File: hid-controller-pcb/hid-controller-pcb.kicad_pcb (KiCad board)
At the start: 4 copper layers, 130.7 x 87.2 mm, 65 parts, among them IC1 RT9080-33GJ5, J1 10118194-0011LF, J2 Jumper, J3 STLink, U1 STM32F103C8Tx, U3 COM-09032, U4 COM-09032, Y1 8MHz, Y2 32.768KHz

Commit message: further work on controller
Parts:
- moved R13 145.3 mm to (255.9, 51.3), turned to 180 degrees
- moved C7 108.8 mm to (200.5, 55.7), turned to 90 degrees
- moved C12 99.0 mm to (212.4, 48.6), turned to -90 degrees
- moved R12 74.5 mm to (157.7, 49.4), turned to -90 degrees
- moved J2 68.7 mm to (205.1, 87.2), turned to 90 degrees
- moved S4 19.8 mm to (151.3, 49.4), turned to -90 degrees
- moved S2 19.5 mm to (170.9, 49.5)
- moved S10 9.44 mm to (208.0, 93.9)
- moved C2 7.12 mm to (214.2, 77.7)
- moved C3 7.12 mm to (214.2, 72.7)
- moved Y2 7.12 mm to (203.1, 74.6)
- moved C4 7.12 mm to (201.5, 69.3)
- moved C5 7.12 mm to (204.5, 69.3)
- moved Y1 7.12 mm to (210.5, 75.3)
- moved C9 5.83 mm to (191.5, 43.5)
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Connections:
- U1 pad 26: DPAD_1 -> BTN_RT
- U1 pad 31: BTN_RT -> DPAD_1
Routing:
- net AN_A1: track 0.00 -> 93.9 mm
- net AN_B1: track 0.00 -> 83.8 mm
- net DPAD_4: track 0.00 -> 79.3 mm, vias 0 -> 1
- net BTN_LT: track 0.00 -> 56.3 mm
- net DPAD_3: track 0.00 -> 55.9 mm, vias 0 -> 1
- net DPAD_1: track 0.00 -> 54.9 mm, vias 0 -> 1
- net AN_B2: track 0.00 -> 52.9 mm
- net DPAD_2: track 0.00 -> 42.7 mm, vias 0 -> 1
- net BOOT0: track 0.00 -> 42.3 mm, vias 0 -> 1
- net AN_A2: track 0.00 -> 36.2 mm
- net AN_SEL1: track 0.00 -> 33.1 mm
- net AN_SEL2: track 0.00 -> 32.1 mm
- net +3V3: track 76.9 -> 55.0 mm, vias 4 -> 7
- net BTN_LB: track 0.00 -> 7.78 mm, vias 0 -> 1
- net Net-(C5-Pad2): track 4.62 -> 12.4 mm
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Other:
- board text added: "SHARE"
- board text added: "START"

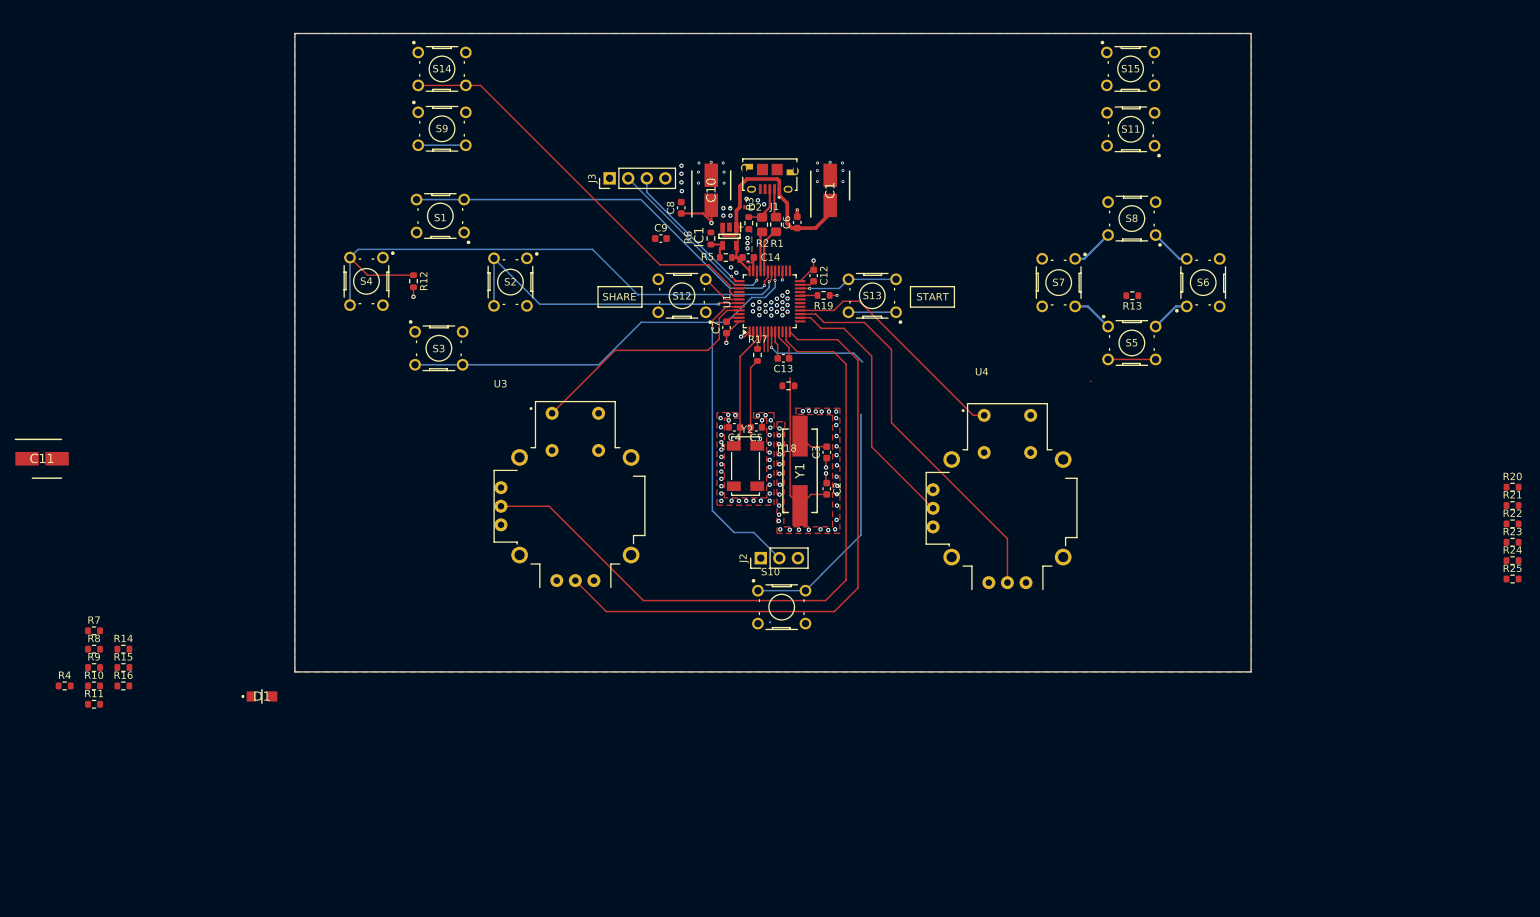
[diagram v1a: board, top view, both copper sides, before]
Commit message: Controller layout done! Reviewing before sending to JLC
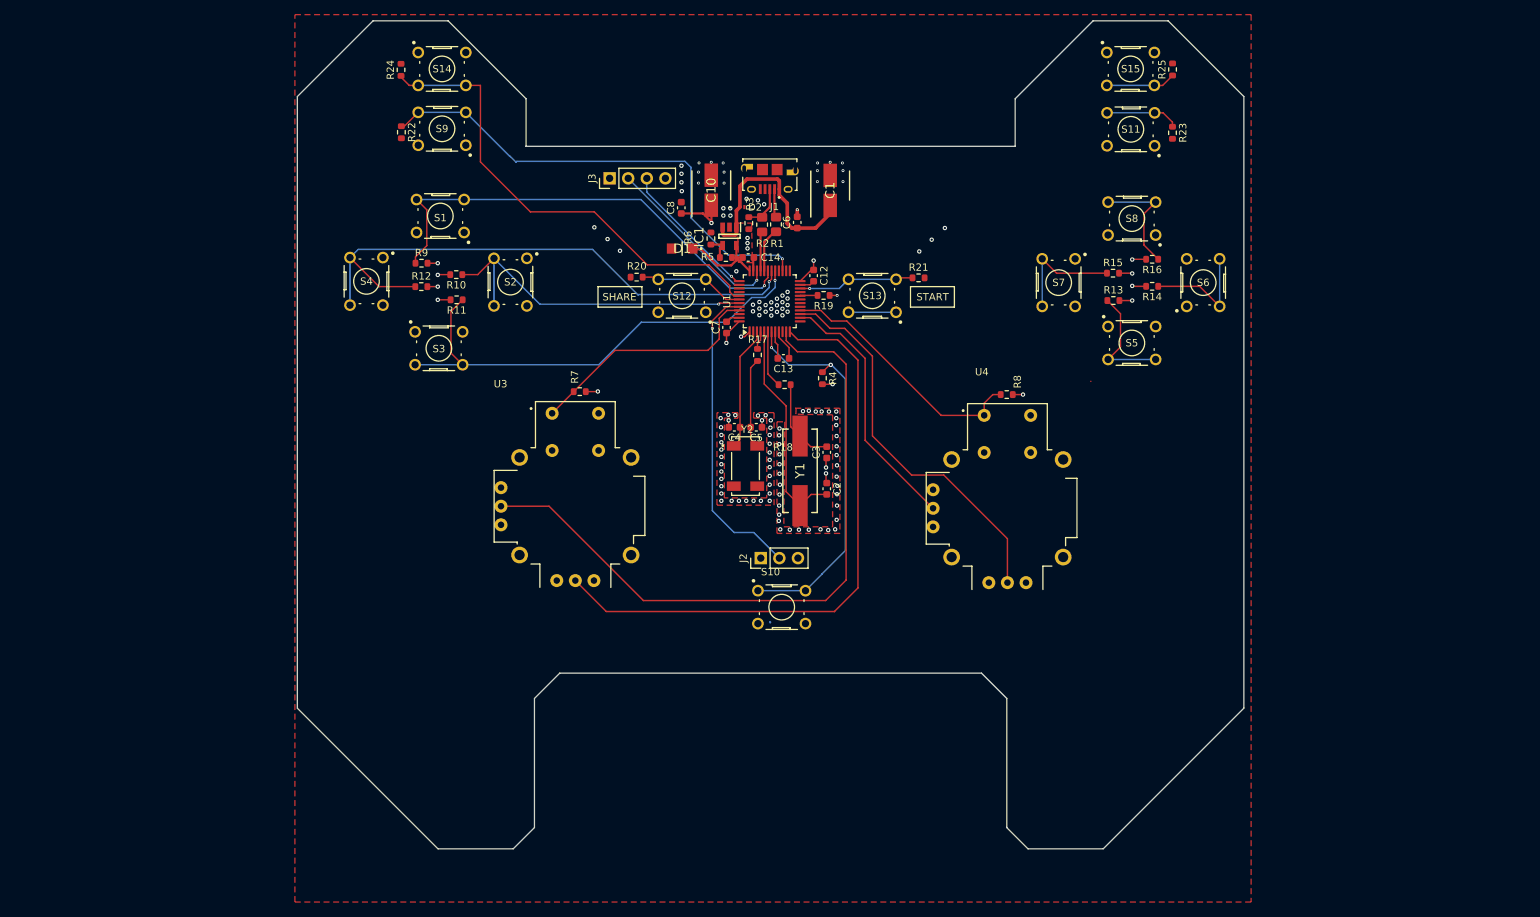
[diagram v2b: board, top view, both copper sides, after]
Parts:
- removed C11: 10uF, lib:CAPAE530X550N
- removed C9: 1uF, Capacitor_SMD:C_0603_1608Metric
- moved R24 166.0 mm to (156.0, 20.5), turned to 90 degrees
- moved R22 161.0 mm to (156.0, 29.0), turned to -90 degrees
- moved R16 152.2 mm to (258.6, 46.4), turned to 180 degrees
- moved R14 149.1 mm to (258.6, 50.1), turned to 180 degrees
- moved R15 145.6 mm to (253.3, 48.3)
- moved R8 129.5 mm to (238.8, 64.8), turned to 180 degrees
- moved R20 123.1 mm to (188.2, 48.8), turned to 180 degrees
- moved R4 111.8 mm to (213.6, 62.6), turned to -90 degrees
- moved R21 86.9 mm to (226.7, 48.9)
- moved D1 83.9 mm to (194.4, 44.9), turned to 180 degrees
- moved R25 83.7 mm to (261.4, 20.4), turned to 90 degrees
- moved R10 74.9 mm to (163.5, 48.5), turned to 180 degrees
- moved R11 74.2 mm to (163.6, 51.9), turned to 180 degrees
- moved R7 74.0 mm to (180.4, 64.5), turned to 180 degrees
- moved R23 72.7 mm to (261.4, 29.1), turned to -90 degrees
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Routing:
- net BTN_LB: track 7.78 -> 66.9 mm
- net BTN_3: track 0.00 -> 16.2 mm
- net BTN_2: track 0.00 -> 16.0 mm
- net BTN_4: track 0.00 -> 15.8 mm
- net GND: track 17.5 -> 29.9 mm, vias 122 -> 134
- net +3V3: track 55.0 -> 44.5 mm, vias 7 -> 10
- net DPAD_3: track 55.9 -> 66.1 mm
- net BTN_RB: track 0.00 -> 10.1 mm
- net DPAD_1: track 54.9 -> 64.8 mm
- net BTN_RT: track 0.00 -> 9.55 mm
- net BTN_1: track 6.50 -> 16.0 mm
- net BTN_LT: track 56.3 -> 65.4 mm
- net BTN_SHR: track 5.72 -> 14.5 mm
- net Net-(C3-Pad2): track 5.32 -> 11.8 mm
- net DPAD_2: track 42.7 -> 47.9 mm
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- removed copper zone on B.Cu, net +3V3
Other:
- board size 130.7 x 87.2 mm -> 129.3 x 113.2 mm

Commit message: final version of controller v1.0
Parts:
- added C15: 0.1uF, Capacitor_SMD:C_0805_2012Metric_Pad1.18x1.45mm_HandSolder, F.Cu at (220.8, 79.1)
- added C16: 0.1uF, Capacitor_SMD:C_0805_2012Metric_Pad1.18x1.45mm_HandSolder, F.Cu at (218.8, 79.1)
- added C17: 0.1uF, Capacitor_SMD:C_0805_2012Metric_Pad1.18x1.45mm_HandSolder, F.Cu at (220.8, 67.9)
- added C18: 0.1uF, Capacitor_SMD:C_0805_2012Metric_Pad1.18x1.45mm_HandSolder, F.Cu at (223.0, 67.9)
- added R26: 10kR, Resistor_SMD:R_0805_2012Metric_Pad1.20x1.40mm_HandSolder, F.Cu at (192.3, 57.4)
- moved R15 2.94 mm to (250.4, 48.6)
- moved R25 2.94 mm to (258.5, 20.7)
- moved S11 2.94 mm to (252.8, 28.9)
- moved S15 2.94 mm to (252.8, 20.7)
- moved S6 2.94 mm to (262.7, 49.9)
- moved R13 2.94 mm to (250.4, 52.3)
- moved R14 2.94 mm to (255.7, 50.4)
- moved R16 2.94 mm to (255.7, 46.7)
- moved S5 2.94 mm to (252.9, 58.1)
- moved S7 2.94 mm to (242.9, 49.9)
- moved S8 2.94 mm to (252.9, 41.1)
- moved R23 2.94 mm to (258.5, 29.4)
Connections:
- J2 pad 2: BOOT0 -> Net-(J2-Pin_2)
- U1 pad 26: BTN_RT -> BTN_RB
- U1 pad 28: BTN_RB -> BTN_RT
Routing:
- net BTN_2: track 16.0 -> 78.6 mm, vias 0 -> 1
- net BTN_RT: track 9.55 -> 62.9 mm, vias 0 -> 1
- net BTN_RB: track 10.1 -> 60.3 mm, vias 0 -> 1
- net BTN_4: track 15.8 -> 60.3 mm, vias 0 -> 1
- net BTN_1: track 16.0 -> 59.0 mm, vias 0 -> 1
- net Net-(J2-Pin_2): track 0.00 -> 41.1 mm, vias 0 -> 1
- net GND: track 29.9 -> 62.5 mm, vias 134 -> 140
- net BTN_3: track 16.2 -> 47.7 mm, vias 0 -> 1
- net BOOT0: track 42.3 -> 10.8 mm, vias 1 -> 0
- net +3V3: track 44.5 -> 54.2 mm, vias 10 -> 13
- net AN_B1: track 83.8 -> 89.7 mm
- net AN_A1: track 93.9 -> 96.4 mm
- net AN_A2: track 35.5 -> 37.1 mm
- added copper zone on B.Cu, net +3V3
- removed copper zone on F.Cu, net +3V3
- removed copper zone on In2.Cu, net GND
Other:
- outline, holes or cut-outs redrawn
- board text added: "A"
- board text added: "B"
- board text added: "Designed by Jonart B"
- board text added: "LB"
- board text added: "LT"
- board text added: "RB"
- board text added: "RESET"
- board text added: "RT"
- board text added: "V"
- board text added: "X"
- board text added: "Y"

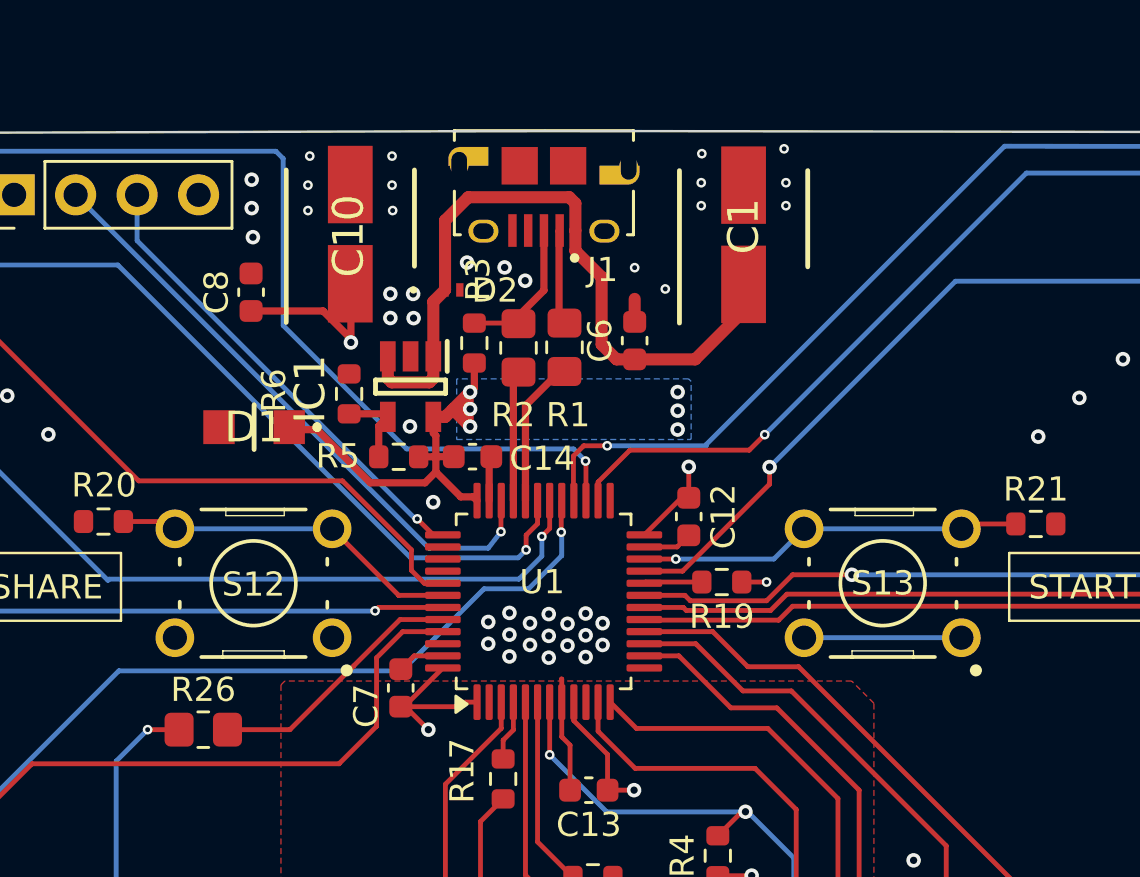
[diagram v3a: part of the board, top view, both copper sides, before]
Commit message: makefile linux gcc path fix
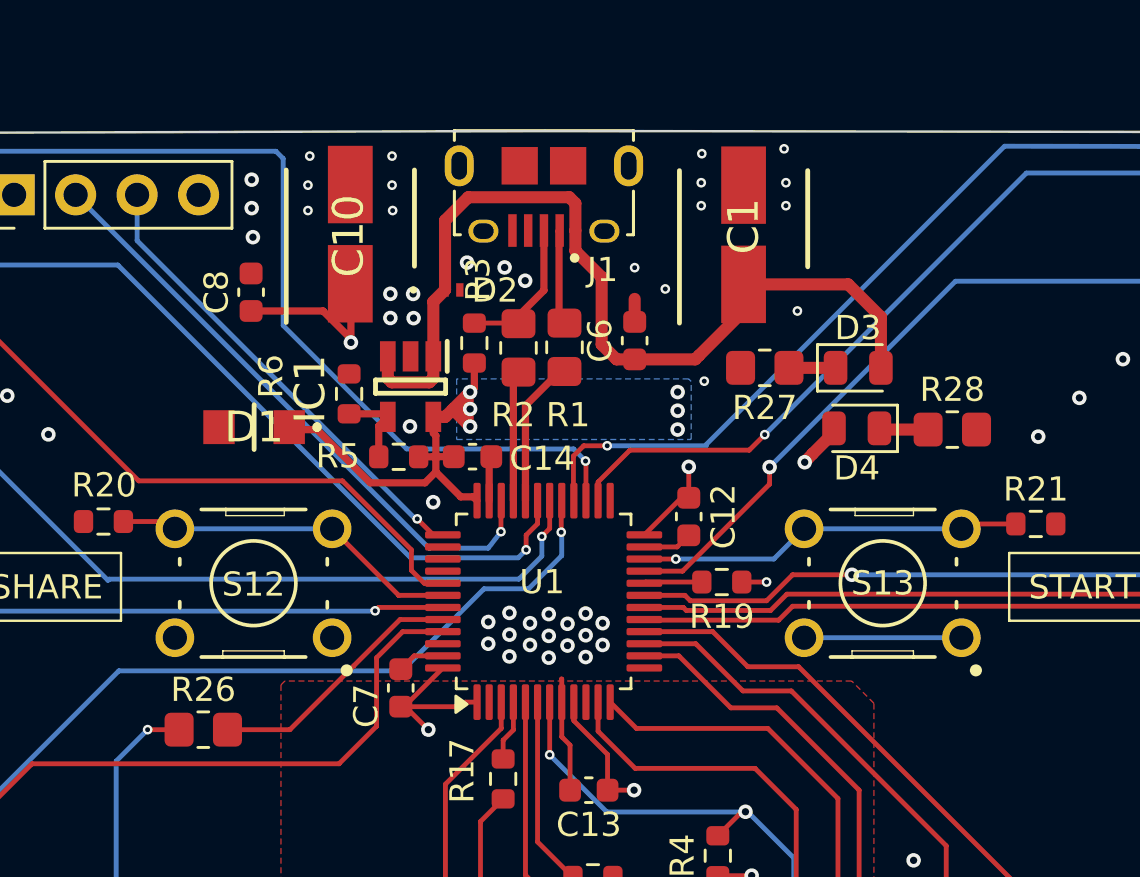
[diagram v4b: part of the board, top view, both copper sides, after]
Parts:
- added D3: LED, LED_SMD:LED_0805_2012Metric, F.Cu at (219.4, 42.5)
- added D4: LED, LED_SMD:LED_0805_2012Metric, F.Cu at (219.3, 45.0)
- added R27: R_Small, Resistor_SMD:R_0805_2012Metric_Pad1.20x1.40mm_HandSolder, F.Cu at (215.5, 42.5)
- added R28: R_Small, Resistor_SMD:R_0805_2012Metric_Pad1.20x1.40mm_HandSolder, F.Cu at (223.2, 45.0)
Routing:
- net +5V: track 28.8 -> 37.1 mm
- net Net-(D4-K): track 0.00 -> 2.03 mm
- net Net-(D3-K): track 0.00 -> 1.93 mm
- net +3V3: track 54.2 -> 56.1 mm, vias 13 -> 14
- net GND: vias 140 -> 142
